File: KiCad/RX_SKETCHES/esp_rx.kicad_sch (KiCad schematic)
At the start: 7 parts, among them U2 ESP32-WROOM-32U

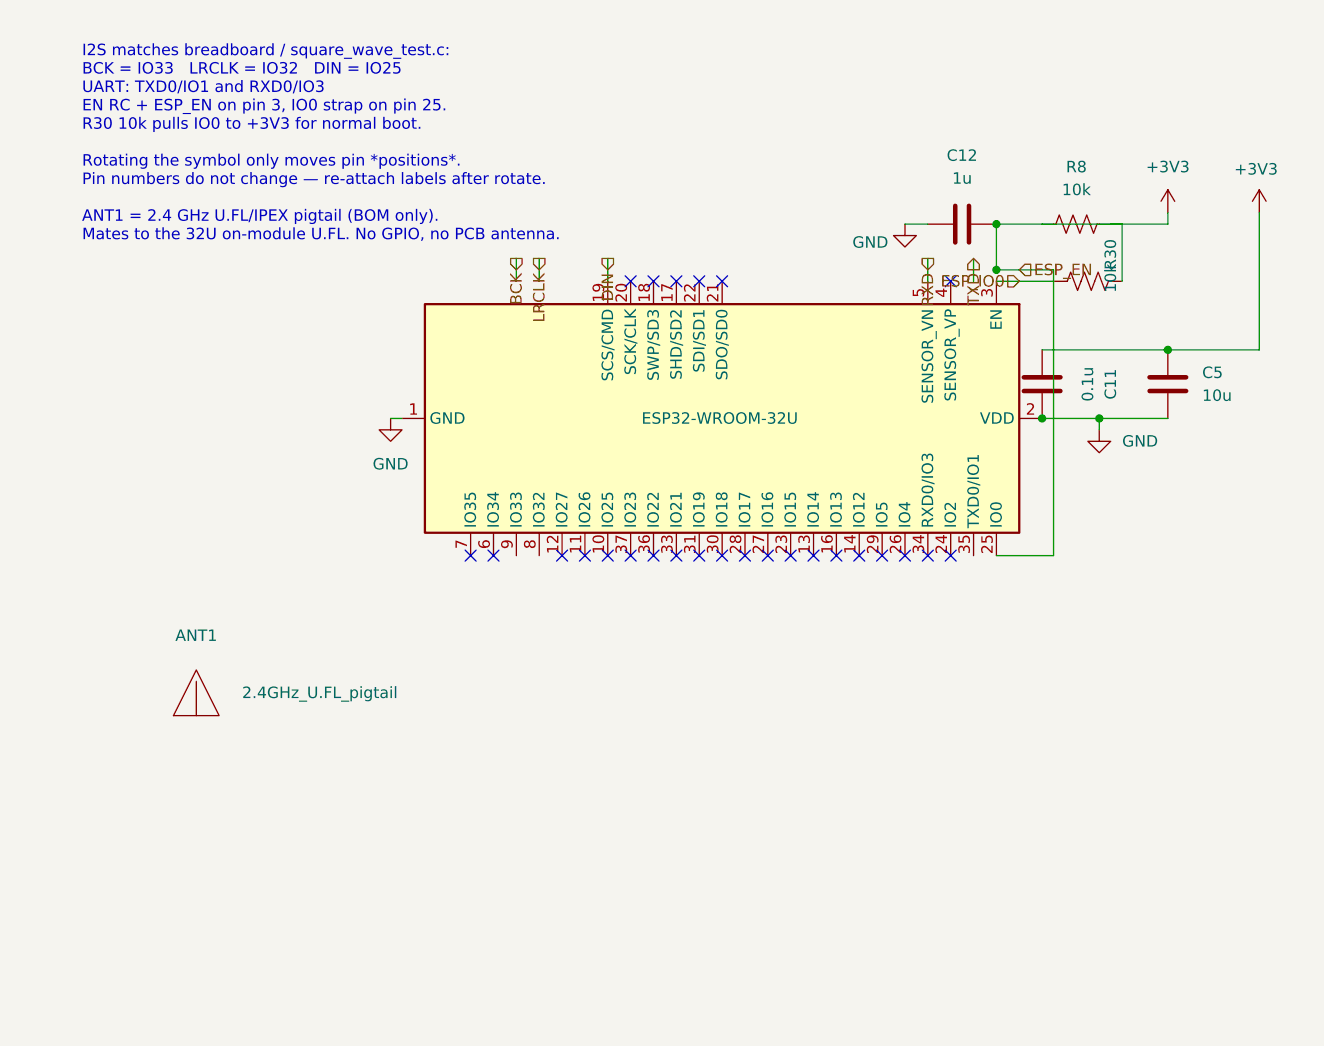
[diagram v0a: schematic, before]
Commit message: WIP: RX schematic review — restore DAC/amp, fix ESP nets, log revisions.
Restore dac/amp from main after rotate damage, rename I2S net to DOUT,
mark amp gain Rs DNP, and record change/rationale in docs/hardware_revisions.org.

Co-authored-by: Cursor <cursoragent@cursor.com>
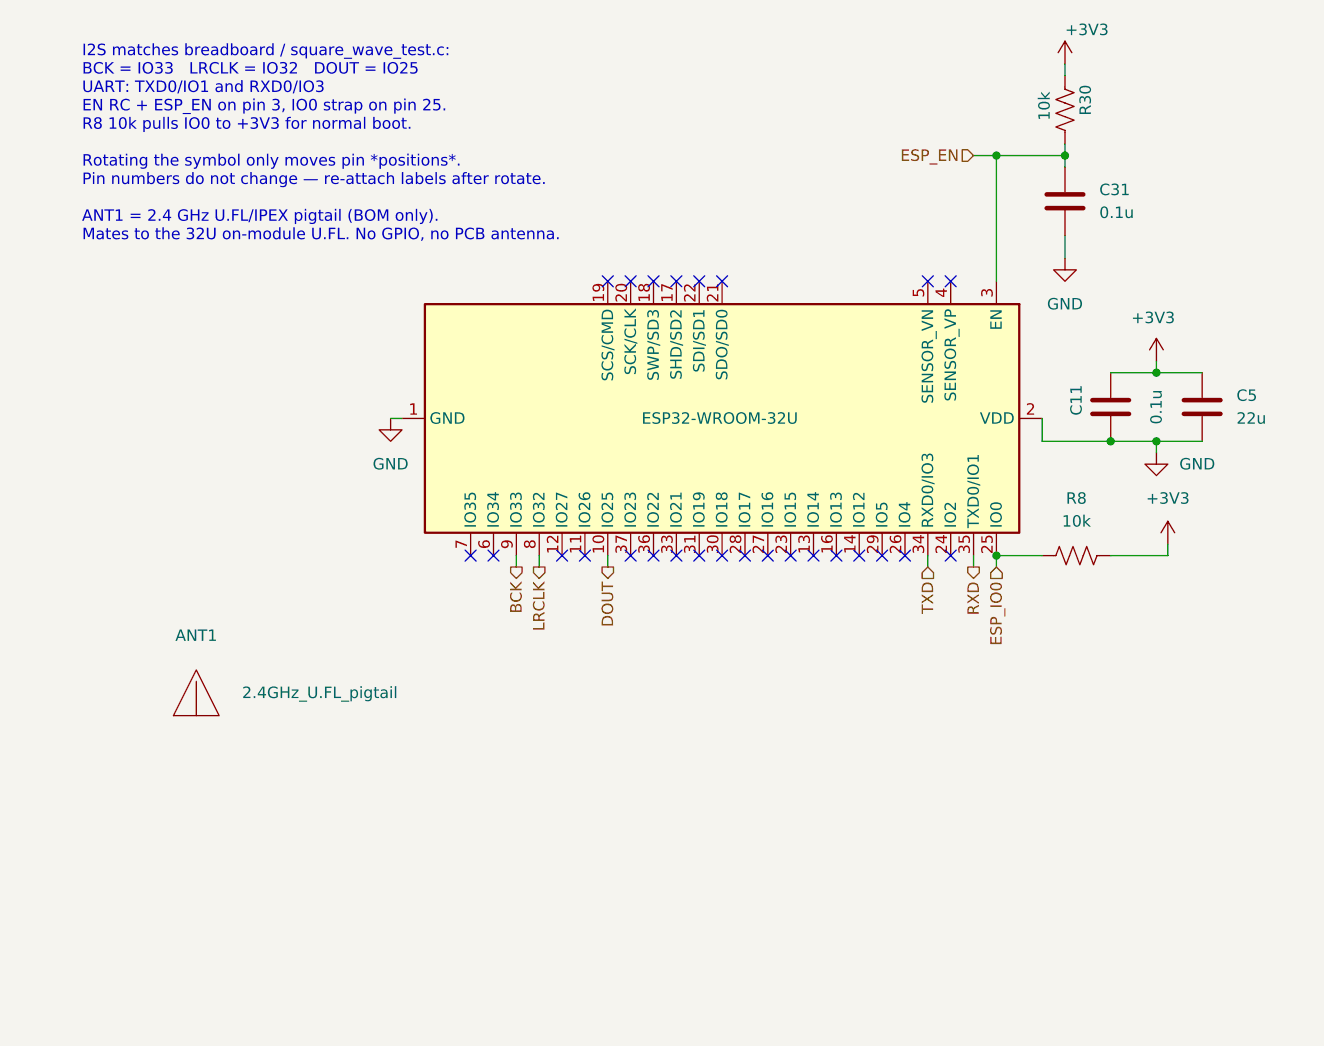
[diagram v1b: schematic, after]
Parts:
- removed C12: 1u, Capacitor_SMD:C_0805_2012Metric_Pad1.15x1.40mm_HandSolder, symbol Device:C
- added C31: 0.1u, symbol Device:C
- C5: value 10u -> 22u
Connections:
- net +3V3: no longer R8.2, U2.25 (IO0)
- net BCK: now also U2.9 (IO33)
- net ESP_IO0: now also R8.2, U2.25 (IO0); no longer R30.1, U2.3 (EN)
- net GND: now also C31.2
- net LRCLK: now also U2.8 (IO32)
- net RXD: now also U2.35 (TXD0/IO1); no longer U2.5 (SENSOR_VN)
- net TXD: now also U2.34 (RXD0/IO3)
- net DOUT: now reaches U2.10 (IO25)
- net DIN: no longer names the net of U2.19 (SCS/CMD)
- new net ESP_EN: C31.1, R30.1, U2.3 (EN)
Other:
- note added: "I2S matches breadboard / square_wave_test.c: BCK = IO33 LRCLK = IO32 DOUT = IO25 UART: TXD0/IO1 and RXD0/IO3 EN RC + ESP_EN on pin 3, IO0 strap on pin 25. R8 10k pulls IO0 to +3V3 for normal boot. Rotating the symbol only moves pin *positions*. Pin numbers do not change — re-attach labels after rotate. ANT1 = 2.4 GHz U.FL/IPEX pigtail (BOM only). Mates to the 32U on-module U.FL. No GPIO, no PCB a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"
- note removed: "I2S matches breadboard / square_wave_test.c: BCK = IO33 LRCLK = IO32 DIN = IO25 UART: TXD0/IO1 and RXD0/IO3 EN RC + ESP_EN on pin 3, IO0 strap on pin 25. R30 10k pulls IO0 to +3V3 for normal boot. Rotating the symbol only moves pin *positions*. Pin numbers do not change — re-attach labels after rotate. ANT1 = 2.4 GHz U.FL/IPEX pigtail (BOM only). Mates to the 32U on-module U.FL. No GPIO, no PCB a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"
- moved on the sheet: C11, C5, R30, R8

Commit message: RX: finish layout, retune gain/coupling, move ESD clamp to unswitched VBUS
Board now passes DRC with zero unconnected items and zero schematic-parity
issues. Remaining 16 violations are footprint-inherent (ESP32 module thermal
via array at 0.2 mm drill, USB-C NPTH-to-pad spacing) and are documented
rather than routed around.

Analog changes, with the reasoning captured in README.org and
docs/hardware_revisions.org so the numbers can be re-checked:

- Gain network populated at RF 4.7k / RIN 47k (-20 dB) instead of DNP 10k.
  Tames the DAC's 2.1 Vrms into sensitive IEMs, unloads the pot taper, and
  moves the coupling corner out of the audible band.
- Coupling caps C1-C4 0.47uF -> 1uF. Corner 7.2 Hz -> 3.4 Hz, and it halves
  the signal developed across the ceramic at 20 Hz, cutting Class-II
  dielectric distortion where it actually occurs.
- D1's third TVS channel moved off the switched +5V rail onto VBUS_RAW. The
  clamp has to sit on the connector pin that is exposed to a finger; behind
  the power switch it went open exactly when the board is most handled.
- SW3 soft mute: XSMT_SEL moved to the throw that puts mute on the south
  slide position. All three switches now follow one rule -- the open throw
  is the safe default (off / quality filter / muted).
- PCM5102 mode pins no longer float: FLT and XSMT get 100k pulldowns, DEMP
  and FMT strap to GND.
- C28 and the four mounting holes added to the schematic to clear parity
  errors against parts that only existed on the PCB.

Also adds a .gitignore so the 24 MB editor .history/ directory and ESP-IDF
build output stop showing up as untracked.

Co-authored-by: Cursor <cursoragent@cursor.com>
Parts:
- added REF1, REF2, REF3, REF4: MountingHole_2.7mm_M2.5, MountingHole:MountingHole_2.7mm_M2.5, symbol Mechanical:MountingHole
- C11, C5: footprint Capacitor_SMD:C_0805_2012Metric_Pad1.15x1.40mm_HandSolder -> Capacitor_SMD:C_0805_2012Metric_Pad1.18x1.45mm_HandSolder
- C31: footprint (none) -> Capacitor_SMD:C_0805_2012Metric_Pad1.18x1.45mm_HandSolder
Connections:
- net +3V3: now also U2.2 (VDD)
- net GND: no longer U2.2 (VDD)
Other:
- moved on the sheet: ANT1
